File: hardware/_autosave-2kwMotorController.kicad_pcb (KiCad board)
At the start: 4 copper layers, 170 x 88 mm, 214 parts, among them M1 MOUNTING_HOLE, M2 MOUNTING_HOLE, M3 MOUNTING_HOLE, M4 MOUNTING_HOLE, M5 MOUNTING_HOLE, M6 MOUNTING_HOLE, P1 CONN_01X02_CBAT, P10 CONN_01_BRK, P11 CONN_01_M+, P12 CONN_01_M-, P13 CONN_01X02_MTMP, P14 CONN_01X02_BTMP, P2 CONN_01X02_FAN, P3 CONN_01X08_DEBUG, P4 CONN_02X05_JTAG, P5 CONN_01X03_UART, P6 CONN_01X03_CAN, P7 CONN_01X05_ENCODER, P8 CONN_01_V+, P9 CONN_01_V-, Q1 DMG4712SSS, Q10 PSMN021-100, Q2 DMG4712SSS, Q3 IRFP4468, Q4 PSMN021-100, Q5 IRFP4468, Q6 IRFP4468, Q7 IRFP4468, Q8 IRFP4468, Q9 IRFP4468, SW2 SW_PUSH, U1 LM358, U10 MCP1501T-30E, U11 PDM1-S, U12 MIC5225-5.0, U13 TM4C1294KCPDT, U14 74LVCH2T45, U15 SN65HVD231D, U16 Si8045AA, U17 MIC4127, U18 MIC4127, U19 LM5102, U2 LAH-100P, U20 Si8045AA, U21 LM5102, U3 LOC110, U4 MCP6001, U5 ADA4805-1, U7 MIC5225-5.0, U8 LT3471, U9 LF33ABDT, Y1 NX5032GA

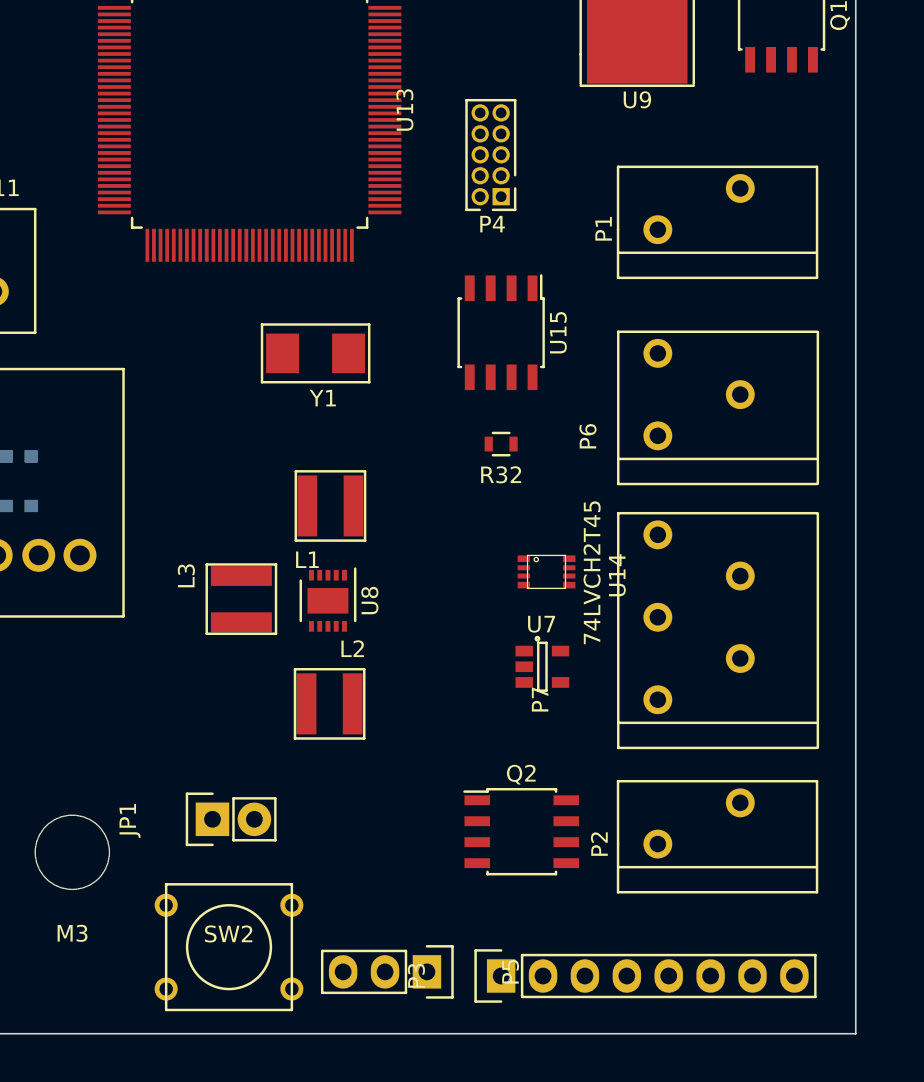
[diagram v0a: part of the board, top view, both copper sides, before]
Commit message: Draft layout of controller section
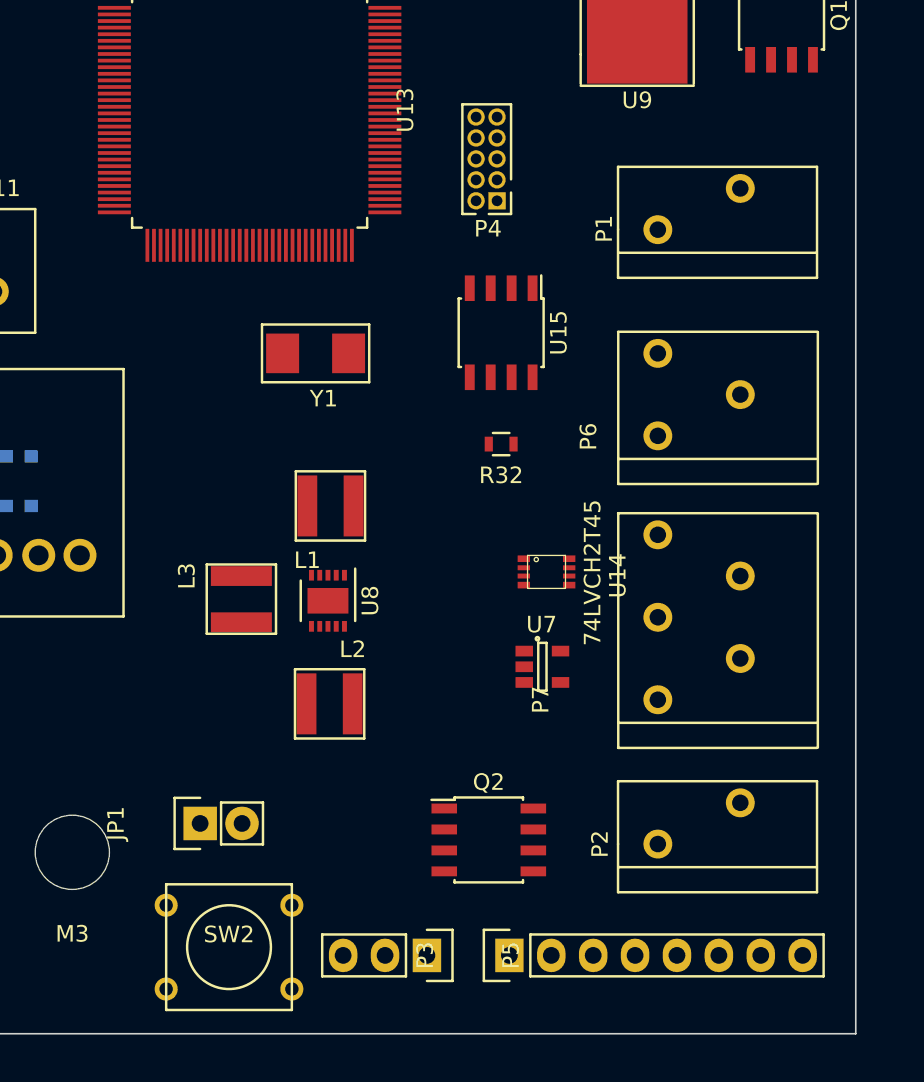
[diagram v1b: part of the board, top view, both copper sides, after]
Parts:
- moved Q2 2.06 mm to (181.2, 104.2)
- moved P3 1.35 mm to (182.5, 111.2)
- moved P5 1.00 mm to (177.5, 111.2)
- moved JP1 0.79 mm to (163.8, 103.2)
- moved P4 0.35 mm to (181.8, 65.5)
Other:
- board text added: "D0 D1 D2 D3 D4 D5 D6 D7"
- board text added: "FACTORY RESET"
- board text added: "RESET"
- board text added: "TX RX GND"
- board text added: "UART"
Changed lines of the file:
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@@
     (area 33.449999 27.949999 203.550001 116.050001)
     (thickness 1.6)
-    (drawings 19)
+    (drawings 24)
     (tracks 209)
     (zones 0)
@@
   )
   (module Pin_Headers:Pin_Header_Straight_1x02 (layer F.Cu)
-    (at 164.5 103 90)
+    (at 163.75 103.25 90)
     (descr "Through hole pin header")
     (tags "pin header")
@@
   )
   (module Housings_SOIC:SOIC-8_3.9x4.9mm_Pitch1.27mm (layer F.Cu)
-    (at 183.25 103.75)
+    (at 181.25 104.25)
     (descr "8-Lead Plastic Small Outline (SN) - Narrow, 3.90 mm Body [SOIC] (see Microchip Packaging Specification 00000049BS.pdf)")
     (tags "SOIC 1.27")
@@
   )
   (module Pin_Headers:Pin_Header_Straight_1x08 (layer F.Cu)
-    (at 182 112.5 90)
+    (at 182.5 111.25 90)
     (descr "Through hole pin header")
     (tags "pin header")
@@
   )
   (module Pin_Headers:Pin_Header_Straight_2x05_Pitch1.27mm (layer F.Cu)
-    (at 182 65.25 180)
+    (at 181.75 65.5 180)
     (descr "Through hole pin header, pitch 1.27mm")
     (tags "pin header")
@@
   )
   (module Pin_Headers:Pin_Header_Straight_1x03 (layer F.Cu)
-    (at 177.5 112.25 270)
+    (at 177.5 111.25 270)
     (descr "Through hole pin header")
     (tags "pin header")
@@
       (net 81 /sensors/BRIDGE_TEMP))
   )
+  (gr_text "FACTORY\nRESET" (at 171.75 103.25) (layer Dwgs.User)
+    (effects (font (size 1 1) (thickness 0.2)))
+  )
+  (gr_text RESET (at 156.75 113.75) (layer Dwgs.User)
+    (effects (font (size 1.5 1.5) (thickness 0.3)))
+  )
+  (gr_text UART (at 175 108.5) (layer Dwgs.User)
+    (effects (font (size 1 1) (thickness 0.2)))
+  )
+  (gr_text "TX RX GND" (at 175.5 114) (layer Dwgs.User)
+    (effects (font (size 1 1) (thickness 0.2)))
+  )
+  (gr_text "D0 D1 D2 D3 D4 D5 D6 D7" (at 191.5 114) (layer Dwgs.User)
+    (effects (font (size 1 1) (thickness 0.2)))
+  )
   (gr_text "2kW DC MOTOR CONTROLLER\nOFD 2017" (at 35.75 112.75) (layer Dwgs.User)
